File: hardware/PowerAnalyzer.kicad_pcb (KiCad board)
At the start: 2 copper layers, 53.4 x 45.7 mm, 68 parts, among them J1 EXPANSION, J10 TEST_IN, J11 PWR_IN, J12 PWR_OUT, J2 UDPI, J3 I2C, J4 FAN_OUT, J5 NTC, J6 UART, J7 USB_C_Receptacle_USB2.0_16P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

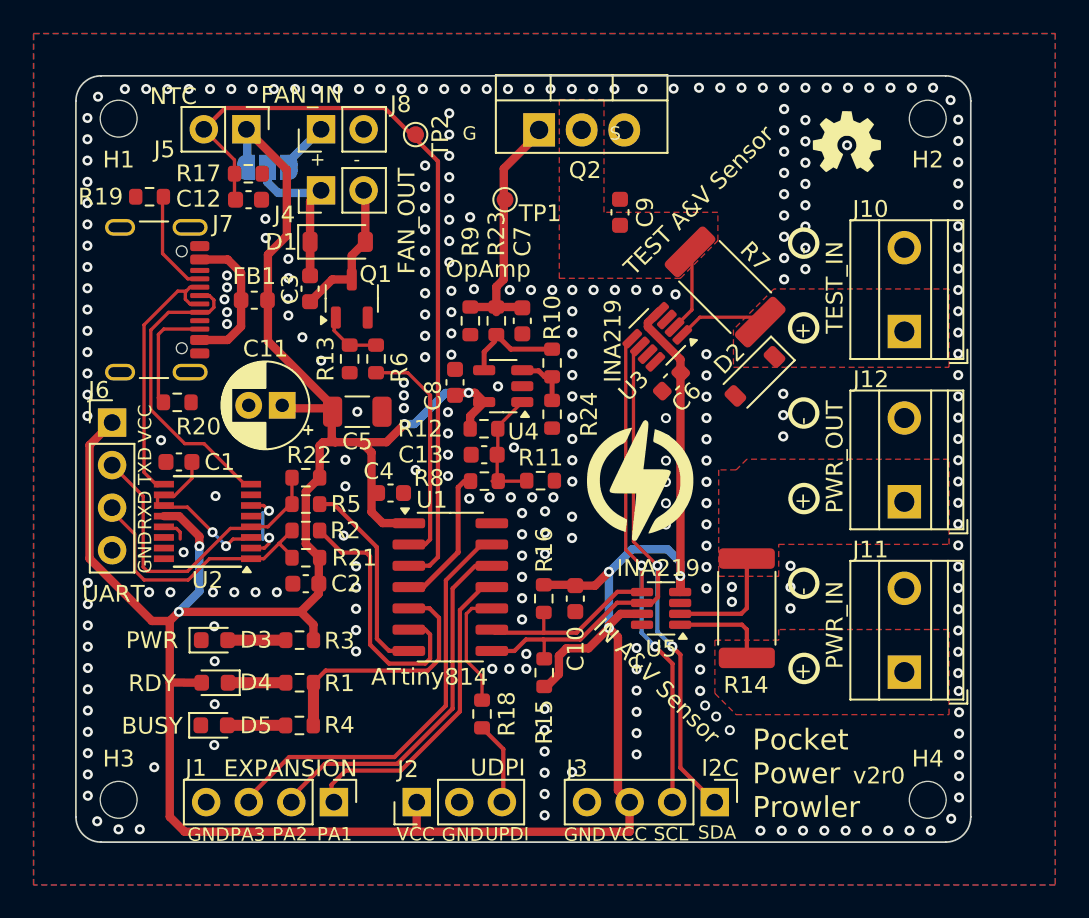
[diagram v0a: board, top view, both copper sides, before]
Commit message: Fix layer names to KiCad
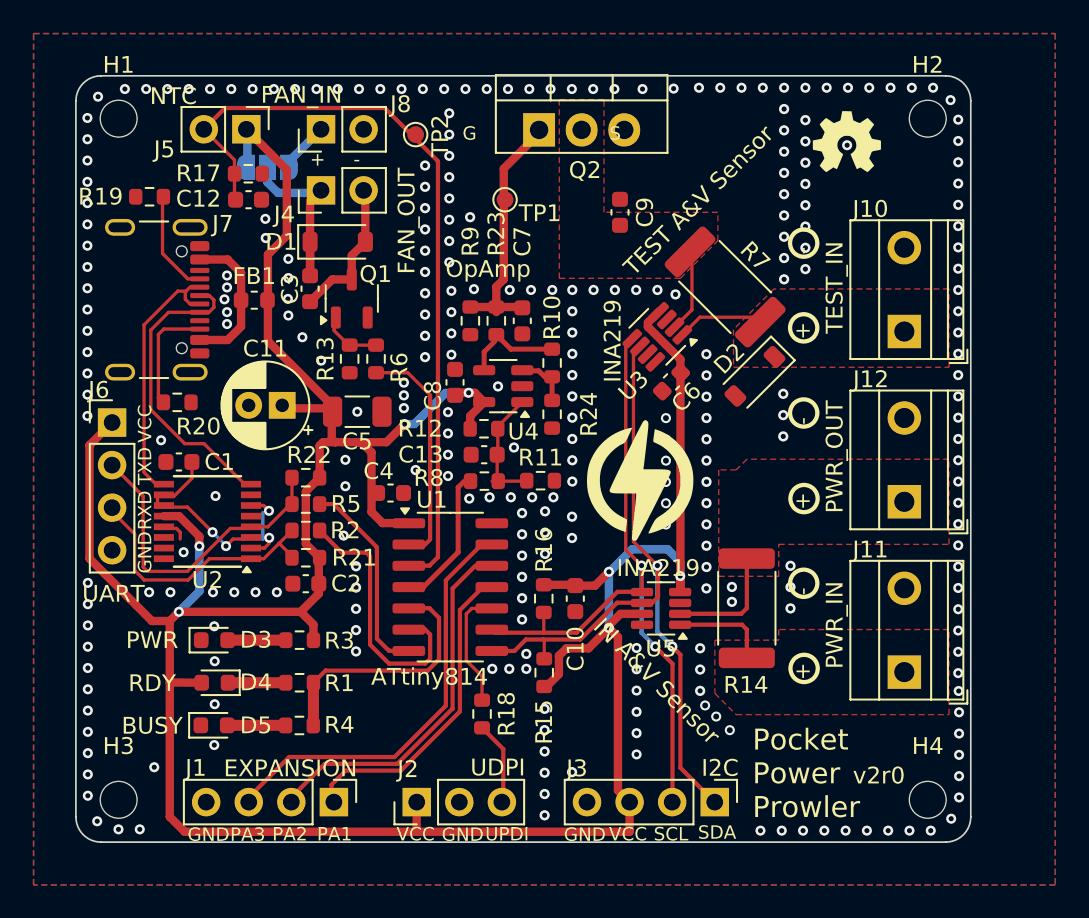
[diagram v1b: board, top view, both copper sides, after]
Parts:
- H1, H2, H3, H4: footprint MountingHole:MountingHole_2.2mm_M2 -> Mechanical:MountingHole_2.2mm_M2_Fiducial
- R11: value 6.8k -> 5.9k
- R23: value 47 -> 100
- R8: value 5.1k -> 5.9k
